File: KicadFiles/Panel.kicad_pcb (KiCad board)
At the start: 2 copper layers, 40.3 x 128.5 mm, 14 parts

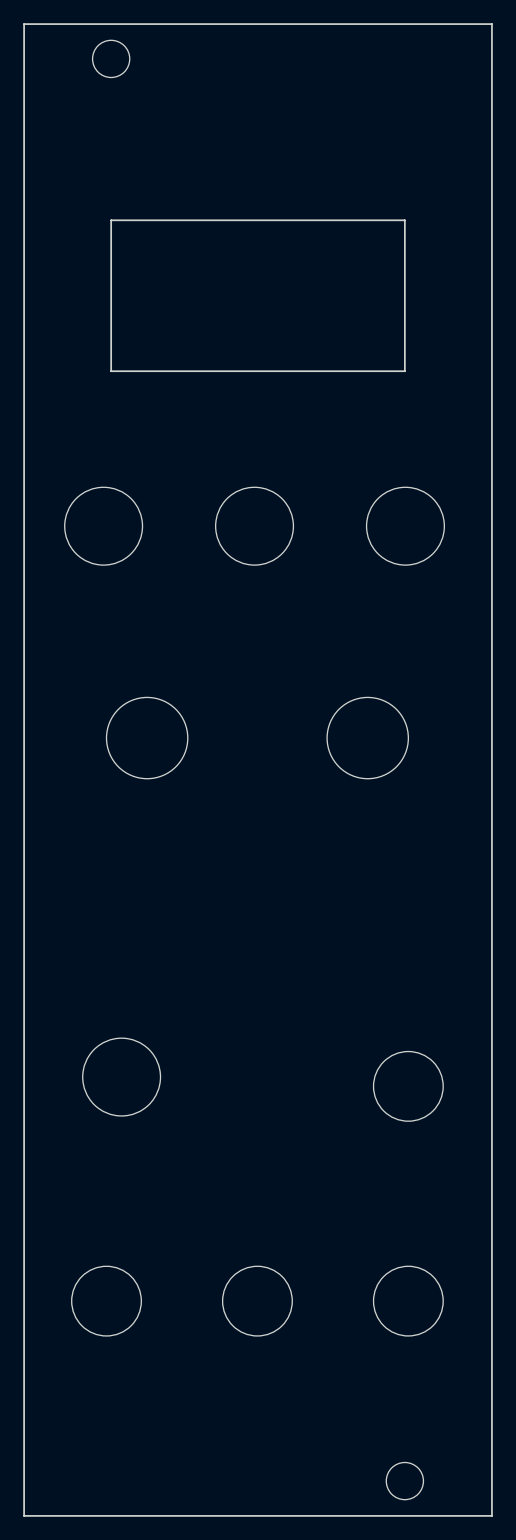
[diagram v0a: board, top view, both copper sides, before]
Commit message: Various code tidy-ups. Added configuration option for encoder direction. ADded new panel gerbers
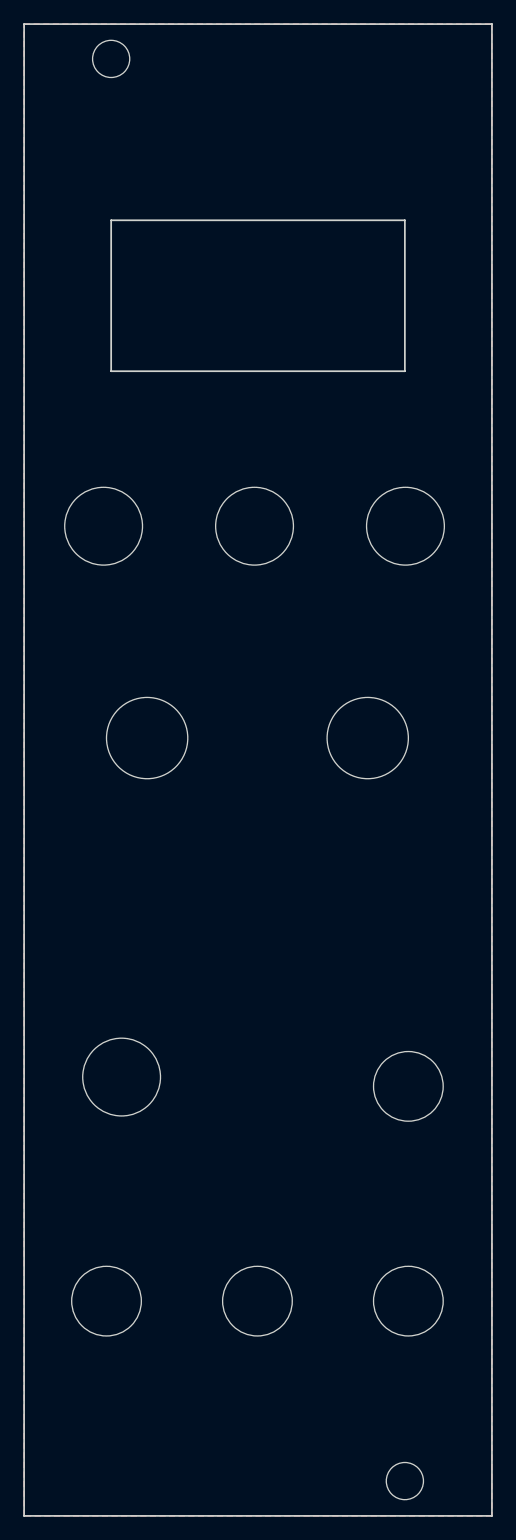
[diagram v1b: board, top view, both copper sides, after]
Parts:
- ?: moved to B.Cu
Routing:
- added copper zone on B.Cu, net (none)
- added copper zone on F.Cu, net (none)
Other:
- board text added: "Lane"
- board text added: "Setup"
- board text removed: "Lane [Setup]"
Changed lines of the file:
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@@
     (area 101.621429 35.025 143.878572 173.575)
     (thickness 1.6)
-    (drawings 19)
+    (drawings 20)
     (tracks 0)
     (zones 0)
@@
     (0 F.Cu signal hide)
     (31 B.Cu signal hide)
-    (32 B.Adhes user)
-    (33 F.Adhes user)
-    (34 B.Paste user)
-    (35 F.Paste user)
+    (32 B.Adhes user hide)
+    (33 F.Adhes user hide)
+    (34 B.Paste user hide)
+    (35 F.Paste user hide)
     (36 B.SilkS user)
-    (37 F.SilkS user)
+    (37 F.SilkS user hide)
     (38 B.Mask user)
     (39 F.Mask user)
-    (40 Dwgs.User user)
-    (41 Cmts.User user)
-    (42 Eco1.User user)
-    (43 Eco2.User user)
+    (40 Dwgs.User user hide)
+    (41 Cmts.User user hide)
+    (42 Eco1.User user hide)
+    (43 Eco2.User user hide)
     (44 Edge.Cuts user)
-    (45 Margin user)
+    (45 Margin user hide)
     (46 B.CrtYd user hide)
     (47 F.CrtYd user hide)
-    (48 B.Fab user)
+    (48 B.Fab user hide)
     (49 F.Fab user hide)
   )
@@
     (trace_clearance 0.2)
     (zone_clearance 0.508)
-    (zone_45_only no)
+    (zone_45_only yes)
     (trace_min 0.2)
     (segment_width 0.2)
@@
     (aux_axis_origin 143.25 79.25)
     (grid_origin 103 40)
-    (visible_elements 7FFEF9FF)
+    (visible_elements 7FFCA601)
     (pcbplotparams
       (layerselection 0x010f0_80000001)
@@
       (plotinvisibletext false)
       (padsonsilk false)
-      (subtractmaskfromsilk false)
+      (subtractmaskfromsilk true)
       (outputformat 1)
       (mirror false)
       (drillshape 0)
       (scaleselection 1)
-      (outputdirectory "C:/Users/Dominic/Pictures/playdice test/"))
+      (outputdirectory "Panel Gerbers/"))
   )
   (net 0 "")
@@
     (pad "" np_thru_hole circle (at 0 0) (size 7 7) (drill 7) (layers *.Cu *.Mask F.SilkS))
   )
-  (module PlayDice:MountingHole_6mm (layer F.Cu)
+  (module PlayDice:MountingHole_6mm (layer B.Cu)
     (at 136 131.5)
     (descr "Mounting Hole 6mm, no annular")
     (tags "mounting hole 6mm no annular")
-    (fp_text reference "" (at 0 -7) (layer F.SilkS) hide
-      (effects (font (size 1 1) (thickness 0.15)))
-    )
-    (fp_text value MountingHole_6mm (at 0 7) (layer F.Fab)
-      (effects (font (size 1 1) (thickness 0.15)))
+    (fp_text reference "" (at 0 7) (layer B.SilkS) hide
+      (effects (font (size 1 1) (thickness 0.15)) (justify mirror))
+    )
+    (fp_text value MountingHole_6mm (at 0 -7) (layer B.Fab)
+      (effects (font (size 1 1) (thickness 0.15)) (justify mirror))
     )
     (fp_circle (center 0 0) (end 2.93 0) (layer Cmts.User) (width 0.15))
-    (fp_circle (center 0 0) (end 6.25 0) (layer F.CrtYd) (width 0.05))
-    (pad 1 np_thru_hole circle (at 0 0) (size 6 6) (drill 6) (layers *.Cu *.Mask F.SilkS))
+    (fp_circle (center 0 0) (end 6.25 0) (layer B.CrtYd) (width 0.05))
+    (pad 1 np_thru_hole circle (at 0 0) (size 6 6) (drill 6) (layers *.Cu *.Mask B.SilkS))
   )
   (module PlayDice:MountingHole_6mm (layer F.Cu)
@@
     (pad "" np_thru_hole circle (at 0 0) (size 3.2 3.2) (drill 3.2) (layers *.Cu *.Mask F.SilkS))
   )
+  (gr_text Setup (at 123 93.6) (layer B.Mask)
+    (effects (font (size 1.5 1.5) (thickness 0.3)) (justify mirror))
+  )
   (gr_text "Mountjoy Modular" (at 122.9 43.1) (layer B.SilkS)
     (effects (font (size 1 1) (thickness 0.25)) (justify mirror))
@@
     (effects (font (size 1.5 1.5) (thickness 0.3)) (justify mirror))
   )
-  (gr_text "Lane\n[Setup]" (at 122.7 92.3) (layer B.SilkS)
+  (gr_text "Lane\n" (at 122.9 89.5) (layer B.SilkS)
     (effects (font (size 1.5 1.5) (thickness 0.3)) (justify mirror))
   )
@@
   (gr_line (start 143.2 40) (end 143.2 168.5) (angle 90) (layer Edge.Cuts) (width 0.15))
   (gr_line (start 102.9 40) (end 143.2 40) (angle 90) (layer Edge.Cuts) (width 0.15))
+  (zone (net 0) (net_name "") (layer B.SilkS) (hatch edge 0.508)
+    (connect_pads (clearance 0.508))
+    (min_thickness 0.254)
+    (fill yes (arc_segments 16) (thermal_gap 0.508) (thermal_bridge_width 0.508))
+    (polygon
+      (pts
+        (xy 126.4 95.5) (xy 119.6 95.5) (xy 119.6 92.2) (xy 126.4 92.2)
+      )
+    )
+  )
+  (zone (net 0) (net_name "") (layer B.Cu) (hatch edge 0.508)
+    (connect_pads (clearance 0.508))
+    (min_thickness 0.254)
+    (fill yes (arc_segments 16) (thermal_gap 0.508) (thermal_bridge_width 0.508))
+    (polygon
+      (pts
+        (xy 102.9 40) (xy 143.2 40) (xy 143.2 168.5) (xy 102.9 168.5)
+      )
+    )
+  )
+  (zone (net 0) (net_name "") (layer F.Cu) (hatch edge 0.508)
+    (connect_pads (clearance 0.508))
+    (min_thickness 0.254)
+    (fill yes (arc_segments 16) (thermal_gap 0.508) (thermal_bridge_width 0.508))
+    (polygon
+      (pts
+        (xy 102.9 40) (xy 143.2 40) (xy 143.2 168.5) (xy 102.9 168.5)
+      )
+    )
+  )
 )
